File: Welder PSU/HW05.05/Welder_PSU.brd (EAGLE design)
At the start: 0 parts

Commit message: Welder PSU HW05.05 Altium -> Eagle Ongoing
Recreating schematic done, Netlisting Ongoing
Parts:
- added C1, C10, C11, C15, C18, C19, C2, C200, C203, C206, C210, C3, C305, C317, C318, C320, C323, C324, C328, C329, C332, C333, C334, C335, C343, C346, C347, C348, C349, C354, C366, C368, C4, C400, C401, C402, C412, C439, C440, C441, C442, C443, C444, C445, C446, C447, C449, C450, C451, C452, C456, C457, C5, C500, C501, C502, C503, C504, C505, C506, C6, C7: 100nF/50V, Labops_Lib_AH:EIA0603
- added C100, C101, C103, C104, C105, C106: SLP152M250H9P3, Labops_Lib_AH:CAPACITOR-ELKO-400V-RM10-35X50
- added C102: R49AN347050B1M, Labops_Lib_AH:R49AN347050B1M
- added C108: ERP610W471MEF0, Labops_Lib_AH:CAP-P12.5-H15-W4-D1
- added C12, C22, C336, C339, C355, C358, C367, C386, C390, C391, C392, C398, C399, C427, C428, C430, C431, C432, C435, C436: 10uF/35V, Labops_Lib_AH:EIA0603
- added C201, C202, C205, C207, C211: 50PX470MEFC10X20, Labops_Lib_AH:CAPACITOR-ELKO-RM5-10X16
- added C300, C351, C352, C353: 470pF/50V, Labops_Lib_AH:EIA0603
- added C301, C311: 12pF/50V, Labops_Lib_AH:EIA0603
- added C302, C312: 510pF/50V, Labops_Lib_AH:EIA0603
- added C303, C304, C307, C308: HVCC153Y6P471MEAX, Labops_Lib_AH:CAPACITOR-FILM-RM12.5MM-12MM
- added C306, C423, C424, C425, C426: 330pF/50V, Labops_Lib_AH:EIA0603
- added C313, C316, C421: 10nF/50V, Labops_Lib_AH:EIA0603
- added C314, C342, C345, C362, C365: 1nF/50V, Labops_Lib_AH:EIA0603
- added C315: 22uF/16V, Labops_Lib_AH:EIA0603
- added C319, C325, C422: 1uF/25V, Labops_Lib_AH:EIA0603
- added C330, C357, C413, C414, C415, C418: 100nF/100V, Labops_Lib_AH:EIA0603
- added C331, C388, C389, C395, C396, C397, C416, C417, C429: 10uF/25V, Labops_Lib_AH:EIA0603
- added C340, C356, C409, C410: 4.7uF/50V, Labops_Lib_AH:EIA0603
- added C344, C453: 1uF/50V, Labops_Lib_AH:EIA0603
- added C350, C369: 2.2uF/35V, Labops_Lib_AH:EIA0603
- added C359, C385: 100nF/25V, Labops_Lib_AH:EIA0603
- added C370, C371, C372, C373, C374, C375, C376, C377, C378, C379, C380, C381: 100pF/50V, Labops_Lib_AH:EIA0603
- added C382, C394: 10F/35V, Labops_Lib_AH:EIA0603
- added C383, C433: 100pF/25V, Labops_Lib_AH:EIA0603
- added C384: 4.7uF/35V, Labops_Lib_AH:EIA0603
- added C393: 470uF/35V, Labops_Lib_AH:CAPACITOR-ELKO-RM5-10X16
- added C419, C420: CK45-B3FD102KYVNA, Labops_Lib_AH:C_DISC_P7.5D12
- added C437, C438: ECW-F4245JLB, Labops_Lib_AH:CAPACITOR-FILM-RM17.5-28X17.5X25
- added C448, C454, C455: 1uF/35V, Labops_Lib_AH:EIA0603
- added C458: 10uF/16V, Labops_Lib_AH:EIA0603
- added D1, D315, D317, D319, D320, D322: SD103AW, Labops_Lib_AH:SOD-323
- added D100, D103: RS1M-13-F, Labops_Lib_AH:SMA-DIODE
- added D101: GBPC3510W, Labops_Lib_AH:GBPC3510W
- added D102: 1N5387BRLG, Labops_Lib_AH:DO-201AD
- added D104, D105: 1N4739A, Labops_Lib_AH:DO-201AD
- added D2, D302, D316, D318: SS14, Labops_Lib_AH:SMA
- added D200, D201: 26-21/GPC-F3138B/CA, Labops_Lib_AH:SMD1206-LED
- added D300, D303, D304, D305, D323, D4: STTH1R04USMB, Labops_Lib_AH:SMB
- added D307, D308, D309, D310, D311, D312: FEP30DP-E3/45TO-247AD, Labops_Lib_AH:TO-247AD
- added D313, D413: GB02SLT12-214, Labops_Lib_AH:SMB
- added D324: BAT54S, Labops_Lib_AH:SOT23DUALDIODE
- added IC1: UCC28951PWR, Labops_Lib_AH:TSSOP24
- added IC100: PC817, Labops_Lib_AH:DIP04
- added IC2, IC301, IC302: LMV641, Labops_Lib_AH:SOT-23-5
- added IC306, IC307, IC310, IC311: UCC21710, Labops_Lib_AH:SOIC16_WIDE_HV
- added IC308, IC309: MAX764CSA+, Labops_Lib_AH:SOIC8
- added IC312, IC313: LM317AEMP, Labops_Lib_AH:SOT223_LM317AEMP
- added IC401: CSTNE8M00G520000R0, Labops_Lib_AH:CSTNE8M00G520000R0
- added IC500: SN65HVD3082EDR, Labops_Lib_AH:SOIC8
- added K100, K101: PANASONIC_ALFG2PF09PANASONIC_ALFG2PF09_0_0, Labops_Lib_AH:PANASONIC_ALFG2PF09_0
- added L300, L302, L304, L308, L309: BLM18RK601SN1D, Labops_Lib_AH:0603
- added L303, L307: SRN8040TA-220M, Labops_Lib_AH:SRN8040TA-220M
- added Q1, Q2, Q300, Q306, Q307, Q308, Q309, Q310, T500, T501, T502: 2N7002, Labops_Lib_AH:SOT23
- added Q100: BC640TA, Labops_Lib_AH:TO-92
- added Q101: KSD1616AYTA, Labops_Lib_AH:TO-92
- added Q500, Q502, Q504: DMP6185SEQ-13, Labops_Lib_AH:SOT223
- added Q501, Q503, Q505, Q506, Q507: BC817, Labops_Lib_AH:SOT23
- added R1, R11, R12, R4, R447, R448, R5, R502, R506, R508, R511, R513, R517, R518, R521, R523, R524, R528: 100R 1%, Labops_Lib_AH:EIA0603
- added R10, R14, R2, R305, R306, R307, R336, R350, R351, R363, R366, R386, R388, R449, R463, R500, R501, R503, R505, R507, R510, R512, R514, R515, R516, R519, R6: 10K 1%, Labops_Lib_AH:EIA0603
- added R100, R112: B57364S100M54, Labops_Lib_AH:VARISTOR_D25_P7.5
- added R101, R103, R111: R_1206EIA1206, Labops_Lib_AH:EIA1206
- added R102, R104: ERG-2SJ513, Labops_Lib_AH:ERG-2S
- added R105: 82K 1%, Labops_Lib_AH:R2010
- added R106: 0R, Labops_Lib_AH:EIA0603
- added R107, R109: 330R 1%, Labops_Lib_AH:EIA0603
- added R108, R113: R_2010EIA2010, Labops_Lib_AH:EIA2010
- added R110: 220K 1%, Labops_Lib_AH:EIA0603
- added R114, R115, R326, R398: RNF12FTD10M0, Labops_Lib_AH:RES-RM12.5-VR37
- added R13, R353, R361, R373, R379, R381, R526, R527: 0R 1%, Labops_Lib_AH:EIA0603
- added R200, R309, R312, R315, R328, R331, R349, R504, R509: 1K 1%, Labops_Lib_AH:EIA0603
- added R201, R3, R346, R347, R348, R391, R8, R9: 3.3K 1%, Labops_Lib_AH:EIA0603
- added R29, R30, R308, R390, R408, R409, R420, R421: 4.7k 1%, Labops_Lib_AH:EIA0603
- added R300, R334, R345, R365, R368: 100K 1%, Labops_Lib_AH:EIA0603
- added R301, R302, R310, R311, R322, R323, R329, R330: 47R 1%, rcl:R2512
- added R303, R31, R407, R419: 4.7K 1%, Labops_Lib_AH:EIA0603
- added R304, R313, R325, R332, R387, R396: 33R 1%, Labops_Lib_AH:EIA2010
- added R314, R343, R400, R403: 10k 1%, Labops_Lib_AH:EIA0603
- added R316: 12R 1%, Labops_Lib_AH:EIA2512
- added R327, R385: 22R 1%, Labops_Lib_AH:EIA2010
- added R333, R369: 150K 1%, Labops_Lib_AH:EIA0603
- added R335, R344: 1.5K 1%, Labops_Lib_AH:EIA0603
- added R337, R341: 510R 1%, Labops_Lib_AH:EIA0603
- added R338, R399, R402: 33K 1%, Labops_Lib_AH:EIA0603
- added R339: 162R 1%, Labops_Lib_AH:EIA0603
- added R340: WSL5931L3000FEA, Labops_Lib_AH:WSLP3921
- added R342: 220k 1%, Labops_Lib_AH:EIA0603
- added R352, R354, R358, R370, R380, R384, R461, R462, R7: 10R 1%, Labops_Lib_AH:EIA0603
- added R355, R364, R377, R382, R430, R431: 412R 1%, Labops_Lib_AH:EIA0603
- added R356, R367, R378, R383, R438: 1.2K 1%, Labops_Lib_AH:EIA0603
- added R357, R359: 49.9K 1%, Labops_Lib_AH:EIA0603
- added R360, R362: 65K 1%, Labops_Lib_AH:EIA0603
- added R371, R374: 18K 1%, Labops_Lib_AH:EIA0603
- added R372, R401, R424, R427: 10R 1%, Labops_Lib_AH:EIA2512
- added R375, R376: 620R 1%, Labops_Lib_AH:EIA0603
- added R389: 825K 1%, Labops_Lib_AH:EIA0603
- added R397, R406, R412, R418, R425, R428: 5.6K 1%, Labops_Lib_AH:EIA0603
- added R404, R410, R416, R422: 220R 1%, Labops_Lib_AH:EIA0603
- added R405, R411, R417, R423: 2.2K 1%, Labops_Lib_AH:EIA0603
- added R426, R429: 5.6k 1%, Labops_Lib_AH:EIA0603
- added R432, R433: 3.9K 1%, Labops_Lib_AH:EIA0603
- added R434, R435: 15.8K 1%, Labops_Lib_AH:EIA0603
- added R436: 41K 1%, Labops_Lib_AH:EIA0603
- added R439, R440, R441, R442: RR02J22RTB, Labops_Lib_AH:RES-RM15-RSF1W
- added R520, R522, R525: 470R 1%, Labops_Lib_AH:EIA0603
- added T1: CST206-2A, Labops_Lib_AH:CST206-2A
- added T300, T301, T303, T304: IHW20N120R5, Labops_Lib_AH:TO-247AC
- added TR305: 11-0060-A, Labops_Lib_AH:11-0060-A
- added U2: R7FA6M5BG3CFBLQFP-144-M, Labops_Lib_AH:LQFP-144-M
- added U300, U301: PAD_3MMX6MM, Labops_Lib_AH:PAD-3.0X6.0MM
- added V1, V2, V3, V500, V501, V502, V503, V504: 0603ESDA-24NSMD, Labops_Lib_AH:EIA0603
- added V100, V300: B72205S0271K101B72205S2131K101, Labops_Lib_AH:EPCOS_B72205S0271K101_0
- added X1: WF2549-2WS05S0B01, Labops_Lib_AH:X10_100MIL_2XROW_VERT
- added X100, X101: 01020071Z, Labops_Lib_AH:FUSE_CLIP_01020071Z
- added X200, X201, X202, X203: 726386-2TE_726386-2, Labops_Lib_AH:TE_726386-2
- added X204, X205: MOLEX_206832-0601MOLEX_206832-0601, Labops_Lib_AH:MOLEX_206832-0601
- added X400, X401, X402: 2304-6111-TP, Labops_Lib_AH:X04_100MIL
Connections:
- new net /COMM_RX_EN: R520.2
- new net /DO_COMM_RX_EN: U2.35
- new net /G_DRV_FAULTA: C371.2, IC306.13, R308.2
- new net /G_DRV_FAULTB: C374.2, IC307.13, R408.2
- new net /G_DRV_FAULTC: C377.2, IC310.13, R30.2
- new net /G_DRV_FAULTD: C380.2, IC311.13, R420.2
- new net AI_I_OUT: U2.113
- new net AN_OUTA_H: IC306.4, R325.2
- new net AN_OUTA_L: IC306.6, R327.2
- new net AN_OUTB_H: IC307.4, R304.2
- new net AN_OUTB_L: IC307.6, R313.2
- new net AN_OUTC_H: IC310.4, R332.2
- new net AN_OUTC_L: IC310.6, R385.2
- new net AN_OUTD_H: IC311.4, R387.2
- new net AN_OUTD_L: IC311.6, R396.2
- new net A_I_OUT: C433.2, IC301.1, R339.1, R345.2
- new net BCD_A: C500.1, Q501.3
- new net BCD_B: C501.1, Q503.3
- new net BCD_C: C502.1, Q505.3
- new net BCD_D: C506.1, Q507.3
- new net COMM_TX_EN: R522.2
- new net CTRLR_OUTA: IC1.22, R358.1
- new net CTRLR_OUTB: IC1.21, R370.1
- new net CTRLR_OUTC: IC1.20, R380.1
- new net CTRLR_OUTD: IC1.19, R384.1
- new net DBG_TDI: X1.1
- new net DGB_SWDCLK_TCK: U2.72
- new net DGB_SWDIO_TCK: X1.7
- new net DGB_SWDIO_TDO: U2.74
- new net DGB_SWDIO_TMS: U2.73, X1.5
- new net DGB_SWO_TDO: X1.3
- new net DISP1_VCC: Q504.2, Q504.4, V502.2
- new net DISP2_VCC: Q502.2, Q502.4, V501.2
- new net DISP3_VCC: Q500.2, Q500.4, V500.2
- new net DI_G_DRV_RDY: C370.2, C376.2, C400.2, IC306.12, IC310.12, R303.2, R31.2, R448.1, U2.85, X400.2
- new net DI_G_DRV_REDY: C373.2, C379.2, IC307.12, IC311.12, R407.2, R419.2
- new net DI_UART_RX: U2.32
- new net DO_7SEG_BCD_A: R504.2, U2.71
- new net DO_7SEG_BCD_B: R509.2, U2.70
- new net DO_7SEG_BCD_C: R513.2, U2.69
- new net DO_7SEG_BCD_D: U2.66
- new net DO_7SEG_DISP1_EN: R517.2, U2.65
- new net DO_7SEG_DISP2_EN: R508.2, U2.64
- new net DO_7SEG_DISP3_EN: R502.2, U2.63
- new net DO_ABRUPT_I_OFF: R462.1, U2.118
- new net DO_COMM_TX_EN: U2.34
- new net DO_I_SET_PWM: U2.97, V3.2, X401.2
- new net DO_PSFB_CTRL_ON: U2.98
- new net DO_PWM_I_SET: R349.1, R7.1
- new net DO_UART_TX: U2.33
- new net DO_V_SET_PWM: V2.2, X401.3
- new net D_7SEG_BCD_D: R524.2
- new net EA_IN: D2.2, D302.2, R305.2, R336.2, R461.1
- new net GND: C1.1, C10.1, C108.P$1, C11.1, C15.1, C18.1, C19.1, C2.1, C200.1, C201.2, C202.2, C203.1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
- new net GND1: C3.2, C346.2, C4.2, IC2.2, Q2.2, R10.1, R6.1
- new net GND_AUX: C206.1, C207.2, C210.1, C211.1, D200.2, X205.5
- new net G_DRV1_VCC: C332.2, C333.2, IC306.15, L302.2, R303.1, R308.1, R390.1
- new net G_DRV2_VCC: C343.2, C344.2, IC307.15, L304.2, R407.1, R408.1, R409.1
- new net G_DRV3_VCC: C10.2, C11.2, IC310.15, L308.2, R29.1, R30.1, R31.1
- new net G_DRV4_VCC: C18.2, C19.2, IC311.15, L309.2, R419.1, R420.1, R421.1
- new net G_DRV_INA: IC306.10, R353.1, R355.1
- new net G_DRV_INB: IC307.10, R361.1, R364.1
- new net G_DRV_INC: IC310.10, R373.1, R377.1
- new net G_DRV_IND: IC311.10, R381.1, R382.1
- new net MAINS_L: V100.2, X100.1, X100.1-1
- new net MAINS_L_FUSED: C102.2, D101.2, R101.2, X101.1, X101.1-1, X200.1, X200.1-2, X201.1, X201.1-2
- new net MAINS_N: C102.1, C108.P$2, D101.4, R103.1, R114.2, V100.1, X202.1, X202.1-2, X203.1, X203.1-2
- new net N$1: C311.1, C315.2, IC302.4, R333.1, R338.2
- new net N$10: IC1.3, R354.2
- new net N$100: Q100.3, R109.1
- new net N$101: D105.K, Q101.3, R111.2
- new net N$102: IC100.4, R106.2, R109.2
- new net N$103: C103.2, C104.2, C106.2, D101.3, R104.1
- new net N$104: C100.2, C101.2, C103.1, C104.1, C105.2, C106.1
- new net N$105: D201.1, R201.1
- new net N$106: D104.K, R105.1, R107.2
- new net N$107: D200.1, R200.1
- new net N$108: D102.A, R105.2
- new net N$109: D100.C, D102.K
- new net N$11: C324.2, IC1.5
- new net N$110: IC100.1, R107.1, R110.2
- new net N$111: C451.2, U2.15
- new net N$112: C454.1, C456.1, U2.127
- new net N$113: C452.1, U2.92
- new net N$114: IC401.3, R14.2, U2.20
- new net N$115: IC401.1, R13.2, R14.1
- new net N$116: R13.1, U2.19
- new net N$117: C505.2, R521.2, R523.2
- new net N$119: IC500.1, Q506.2
- new net N$12: IC1.2, R352.2
- new net N$120: Q506.1, R516.2
- new net N$121: Q501.1, R504.1
- new net N$123: IC500.2, R520.1
- new net N$124: Q501.2, R506.2
- new net N$125: X1.8
- new net N$127: IC500.3, R522.1
- new net N$128: IC500.4, R525.1
- new net N$129: Q503.1, R509.1
- new net N$13: C320.2, C422.1, IC1.23, L300.1
- new net N$131: Q503.2, R511.2
- new net N$133: Q505.1, R513.1
- new net N$135: Q505.2, R518.2
- new net N$137: Q507.1, R524.1
- new net N$139: Q507.2, R528.2
- new net N$14: IC1.16, R386.1
- new net N$140: R508.1, R510.2, T501.1
- new net N$141: R502.1, R503.2, T500.1
- new net N$142: R501.1, T500.3
- new net N$143: Q500.1, R500.1, R501.2
- new net N$145: R507.1, T501.3
- new net N$147: Q502.1, R505.1, R507.2
- new net N$15: D303.K, R315.1, R316.2
- new net N$150: R517.1, R519.2, T502.1
- new net N$151: R514.1, T502.3
- new net N$152: Q504.1, R512.1, R514.2
- new net N$16: Q307.1, R356.1, R358.2
- new net N$17: IC1.13, R366.2, R375.1
- new net N$18: Q307.2, R353.2, R356.2
- new net N$19: IC1.14, R363.2, R376.1
- new net N$2: IC1.12, R374.2, R379.2
- new net N$20: C421.2, R338.1, R339.2, R342.1, R343.1
- new net N$21: D303.A, T1.2
- new net N$22: Q309.1, R378.1, R380.2
- new net N$23: Q309.2, R373.2, R378.2
- new net N$24: C313.2, R335.2, R337.1
- new net N$25: C313.1, C314.1, C316.2
- new net N$26: C316.1, R341.1, R344.2
- new net N$27: Q308.1, R367.1, R370.2
- new net N$28: Q308.2, R361.2, R367.2
- new net N$29: R323.1, R330.2
- new net N$3: IC1.11, R369.1, R371.1
- new net N$30: C433.1, IC301.4, R341.2, R345.1
- new net N$31: Q306.1, R349.2, R351.2
- new net N$32: C383.2, IC301.3, R334.1, R337.2
- new net N$33: Q310.1, R383.1, R384.2
- new net N$34: R301.1, R310.2
- new net N$35: Q310.2, R381.2, R383.2
- new net N$36: C303.2, R301.2
- new net N$37: C315.1, R342.2
- new net N$38: Q1.1, R462.2, R463.2
- new net N$39: Q306.3, R347.2, R348.1
- new net N$4: IC1.10, R365.1, R368.1
- new net N$40: R302.1, R311.2
- new net N$41: C304.2, R302.2
- new net N$42: C352.1, R330.1, R331.2, T303.3
- new net N$43: R322.1, R329.2
- new net N$44: C307.2, R322.2
- new net N$45: C308.2, R323.2
- new net N$46: C318.1, R346.2, R347.1
- new net N$47: C437.2, C438.2, TR305.1
- new net N$48: D310.1, D310.3, D311.1, D311.3, D312.1, D312.3, TR305.3
- new net N$49: D307.1, D307.3, D308.1, D308.3, D309.1, D309.3, TR305.5
- new net N$5: IC1.9, R362.1
- new net N$50: R440.2
- new net N$51: R439.2, R440.1
- new net N$52: C419.1, R439.1
- new net N$53: C420.1, R442.2
- new net N$54: R441.1
- new net N$55: R441.2, R442.1
- new net N$56: D413.A, R401.1, R427.1
- new net N$57: C317.1, IC302.3, R346.1, R350.2
- new net N$58: IC309.2, R402.2, R403.2
- new net N$59: C423.2, R397.2, R404.2, R425.1
- new net N$6: IC1.8, R360.1
- new net N$60: IC312.1, R430.1, R432.1
- new net N$61: C359.1, IC309.4, R403.1
- new net N$62: IC313.1, R431.1, R433.1
- new net N$63: D318.1, IC309.8, L307.2
- new net N$64: D316.1, IC308.8, L303.2
- new net N$65: C354.1, IC308.4, R400.1
- new net N$66: IC308.2, R399.2, R400.2
- new net N$67: C396.2, C397.2
- new net N$68: D300.A, R404.1
- new net N$69: C424.2, R406.2, R410.2, R426.1
- new net N$7: IC1.6, R357.1
- new net N$70: D313.A, R372.1, R424.1
- new net N$71: C425.2, R412.1, R416.2, R428.2
- new net N$72: D304.A, R416.1
- new net N$73: D4.A, R410.1
- new net N$74: C312.1, R333.2
- new net N$75: R306.1, R307.2, R314.1
- new net N$76: Q1.3, R461.2
- new net N$77: C311.2, C312.2, D2.1, IC302.1, R336.1
- new net N$78: C305.1, R314.2
- new net N$79: Q2.1, R6.2, R7.2
- new net N$8: IC1.7, R359.1
- new net N$80: Q2.3, R3.1, R8.2
- new net N$81: C3.1, R8.1, R9.2
- new net N$82: C4.1, IC2.3, R10.2, R9.1
- new net N$83: C426.2, R418.2, R422.2, R429.1
- new net N$84: D305.A, R422.1
- new net N$85: C301.1, C305.2, IC2.4, R300.1, R306.2
- new net N$86: C302.1, R300.2
- new net N$87: C301.2, C302.2, D302.1, IC2.1, R305.1
- new net N$88: C416.1, R307.1, R434.2
- new net N$89: C417.1, R2.1, R434.1, R435.1
- new net N$9: IC1.4, R354.1
- new net N$90: R435.2, R436.2, R438.2
- new net N$91: R114.1, R115.2
- new net N$92: D323.K, R436.1
- new net N$93: D101.1, K100.4, K101.4, R100.1, R112.1
- new net N$94: C415.2, C418.1
- new net N$95: D103.C, K100.2, K101.2, Q101.1
- new net N$96: R101.1, R103.2
- new net N$97: D103.A, K100.1, K101.1, Q100.1, R106.1
- new net N$98: Q101.2, R108.2, R113.2
- new net N$99: R102.1, R104.2
- new net NDI_G_DRV_FAULTA: C1.2, R4.1, U2.89, X402.1
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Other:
- board outline added: 160 x 100 mm

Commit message: Welder PSU HW05.05
Translated to Eagle, Design Rule Check still open
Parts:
- removed C1, C10, C11, C15, C18, C19, C2, C3, C4, C5, C6, C7: 100nF/50V, Labops_Lib_AH:EIA0603
- removed C12, C22: 10uF/35V, Labops_Lib_AH:EIA0603
- removed D1: SD103AW, Labops_Lib_AH:SOD-323
- removed D2: SS14, Labops_Lib_AH:SMA
- removed D4: STTH1R04USMB, Labops_Lib_AH:SMB
- removed D413: GB02SLT12-214, Labops_Lib_AH:SMB
- removed IC2: LMV641, Labops_Lib_AH:SOT-23-5
- removed Q1, Q2, Q307, Q308, Q309, Q310: 2N7002, Labops_Lib_AH:SOT23
- removed R1, R11, R12, R4, R5: 100R 1%, Labops_Lib_AH:EIA0603
- removed R10, R14, R2, R6: 10K 1%, Labops_Lib_AH:EIA0603
- removed R13: 0R 1%, Labops_Lib_AH:EIA0603
- removed R29, R30: 4.7k 1%, Labops_Lib_AH:EIA0603
- removed R3, R8, R9: 3.3K 1%, Labops_Lib_AH:EIA0603
- removed R31: 4.7K 1%, Labops_Lib_AH:EIA0603
- removed R7: 10R 1%, Labops_Lib_AH:EIA0603
- removed T1: CST206-2A, Labops_Lib_AH:CST206-2A
- removed U2: R7FA6M5BG3CFBLQFP-144-M, Labops_Lib_AH:LQFP-144-M
- removed V1, V2, V3: 0603ESDA-24NSMD, Labops_Lib_AH:EIA0603
- added C204, C309, C310, C338, C361, C363, C364, C403, C404, C405, C407, C411: 100nF/50V, Labops_Lib_AH:EIA0603
- added C337: 1uF/25V, Labops_Lib_AH:EIA0603
- added C360: 1uF/35V, Labops_Lib_AH:EIA0603
- added C387: 100nF/100V, Labops_Lib_AH:EIA0603
- added C408, C434: 10uF/35V, Labops_Lib_AH:EIA0603
- added D301: STTH1R04USMB, Labops_Lib_AH:SMB
- added D306: SS14, Labops_Lib_AH:SMA
- added D314: GB02SLT12-214, Labops_Lib_AH:SMB
- added D321: SD103AW, Labops_Lib_AH:SOD-323
- added IC300: LMV641, Labops_Lib_AH:SOT-23-5
- added IC400: R7FA6M5BG3CFBLQFP-144-M, Labops_Lib_AH:LQFP-144-M
- added R317, R318, R319, R320, R321, R324, R450: 10K 1%, Labops_Lib_AH:EIA0603
- added R413: 4.7K 1%, Labops_Lib_AH:EIA0603
- added R414, R415: 4.7k 1%, Labops_Lib_AH:EIA0603
- added R437: 100K 1%, Labops_Lib_AH:EIA0603
- added R443, R444, R445, R446, R452: 100R 1%, Labops_Lib_AH:EIA0603
- added R451: 0R 1%, Labops_Lib_AH:EIA0603
- added T302, T307, T308, T309, T310, T313: 2N7002, Labops_Lib_AH:SOT23
- added TR300: CST206-2A, Labops_Lib_AH:CST206-2A
- added V400, V401, V402: 0603ESDA-24NSMD, Labops_Lib_AH:EIA0603
- added X2, X4: 7461061, Labops_Lib_AH:X01_M10_7461061
- added X3: 726386-2TE_726386-2, Labops_Lib_AH:TE_726386-2
- added X403: WF2549-2WS05S0B01, Labops_Lib_AH:X10_100MIL_2XROW_VERT
- added X5, X6: 615008148521, Labops_Lib_AH:615008148521
- added X7, X8: 2304-6111-TP, Labops_Lib_AH:X04_100MIL
- C108: device Labops_Lib_AH:CAP-P12.5-H15-W4-D1 -> Labops_Lib_AH:CAPACITOR-FILM-RM12.5MM-12MM
- R309, R312, R328, R331, R436, R438: device Labops_Lib_AH:EIA0603 -> Labops_Lib_AH:EIA2010
- X1: value WF2549-2WS05S0B01 -> 726386-2TE_726386-2; device Labops_Lib_AH:X10_100MIL_2XROW_VERT -> Labops_Lib_AH:TE_726386-2
- moved R340 624.7 mm to (348.9, 16.9), turned to 180 degrees
- moved V300 591.8 mm to (297.1, 11.8), turned to 180 degrees
- moved R439 581.2 mm to (256.0, 48.3), turned to 90 degrees
- moved V502 581.0 mm to (189.7, 5.24)
- moved V501 578.4 mm to (181.1, 5.24)
- moved R512 577.3 mm to (185.3, 11.1), turned to 90 degrees
- moved V500 576.0 mm to (172.4, 5.24)
- moved R514 567.3 mm to (185.3, 7.78), turned to 90 degrees
- moved Q504 562.8 mm to (189.6, 10.3)
- moved R519 554.2 mm to (163.5, 7.53), turned to 270 degrees
- moved R505 549.3 mm to (176.7, 11.1), turned to 90 degrees
- moved R517 547.3 mm to (165.1, 7.53), turned to 90 degrees
- moved R507 539.8 mm to (176.7, 7.78), turned to 90 degrees
- moved Q502 535.7 mm to (181.0, 10.3)
- moved C352 535.2 mm to (262.8, 140.0), turned to 90 degrees
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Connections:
- net VDC360V renamed NODE-A
- removed net /COMM_RX_EN: R520.2
- removed net A_I_OUT: C433.2, IC301.1, R339.1, R345.2
- removed net COMM_TX_EN: R522.2
- removed net DGB_SWDCLK_TCK: U2.72
- removed net DGB_SWO_TDO: X1.3
- removed net DI_G_DRV_REDY: C373.2, C379.2, IC307.12, IC311.12, R407.2, R419.2
- removed net DO_PWM_I_SET: R349.1, R7.1
- removed net D_7SEG_BCD_D: R524.2
- removed net GND1: C3.2, C346.2, C4.2, IC2.2, Q2.2, R10.1, R6.1
- removed net GND_AUX: C206.1, C207.2, C210.1, C211.1, D200.2, X205.5
- removed net N$125: X1.8
- removed net N$50: R440.2
- removed net N$54: R441.1
- removed net N$99: R102.1, R104.2
- removed net NDI_G_DRV_FAULTA: C1.2, R4.1, U2.89, X402.1
- removed net NDI_G_DRV_FAULTB: C2.2, R5.1, U2.88, X402.2
- removed net NDI_G_DRV_FAULTC: C5.2, R11.1, U2.87, X402.3
- removed net NDI_G_DRV_FAULTD: C6.2, R12.1, U2.86, X402.4
- removed net NODE_B: C335.1, C336.1, C345.1, C349.1, C350.1, C382.1, C392.1, C424.1, D317.A, IC307.3, R411.2
- removed net NODE_D: C22.1, C365.1, C366.1, C367.1, C368.1, C369.1, C393.2, C394.1, C426.1, D320.A, IC311.3, R423.2
- removed net UART_RX: Q506.3, R515.2
- removed net UART_TX: R525.2
- removed net VDD_B: R406.1
- removed net VDD_D: R418.1
- removed net VEE_B: C349.2, C350.2, C392.2, IC307.8
- removed net VEE_D: C22.2, C368.2, C369.2, IC311.8
- removed net V_RECT_F_MIN: D104.A, IC100.2, R110.1
- new net N$118: IC307.1
- net /DO_COMM_RX_EN: now also IC400.32, R520.2; no longer U2.35
- net /G_DRV_FAULTA: now also C404.2, IC400.89, R445.1, X402.1
- net /G_DRV_FAULTB: now also C405.2, IC400.88, R443.1, X402.2
- net /G_DRV_FAULTC: now also C403.2, IC400.87, R414.2, R446.1, X402.3; no longer R30.2
- net /G_DRV_FAULTD: now also C407.2, IC400.86, R444.1, X402.4
- net AI_I_OUT: now also C433.2, IC301.1, IC400.113, R339.1, R345.2; no longer U2.113
- net BCD_A: now also X8.1
- net BCD_B: now also X8.2
- net BCD_C: now also X8.3
- net BCD_D: now also X8.4
- net DBG_TDI: now also IC400.75, X403.1; no longer X1.1
- net DGB_SWDIO_TCK: now also IC400.72, X403.7; no longer X1.7
- net DGB_SWDIO_TDO: now also IC400.74, X403.3; no longer U2.74
- net DGB_SWDIO_TMS: now also IC400.73, X403.5; no longer U2.73, X1.5
- net DISP1_VCC: now also X7.1
- net DISP2_VCC: now also X7.2
- net DISP3_VCC: now also X7.3
- net DI_G_DRV_RDY: now also C373.2, C379.2, IC307.12, IC311.12, IC400.85, R407.2, R413.2, R419.2; no longer R31.2, U2.85
- net DI_UART_RX: now also IC400.35, Q506.3, R515.2; no longer U2.32
- net DO_7SEG_BCD_A: now also IC400.71; no longer U2.71
- net DO_7SEG_BCD_B: now also IC400.70; no longer U2.70
- net DO_7SEG_BCD_C: now also IC400.69; no longer U2.69
- net DO_7SEG_BCD_D: now also IC400.66, R524.2; no longer U2.66
- net DO_7SEG_DISP1_EN: now also IC400.65; no longer U2.65
- net DO_7SEG_DISP2_EN: now also IC400.64; no longer U2.64
- net DO_7SEG_DISP3_EN: now also IC400.63; no longer U2.63
- net DO_ABRUPT_I_OFF: now also IC400.118; no longer U2.118
- net DO_COMM_TX_EN: now also IC400.33, R522.2; no longer U2.34
- net DO_I_SET_PWM: now also IC400.97, R349.1, V401.2; no longer U2.97, V3.2
- net DO_PSFB_CTRL_ON: now also IC400.98; no longer U2.98
- net DO_UART_TX: now also IC400.34, R525.2; no longer U2.33
- net DO_V_SET_PWM: now also R320.1, V402.2; no longer V2.2
- net EA_IN: now also D306.2; no longer D2.2
- net GND: now also C108.1, C204.1, C309.2, C310.2, C337.2, C338.1, C346.2, C360.1, C361.1, C363.1, C364.1, C403.1, C404.1, C405.1, C407.1, IC300.2, IC400.100, IC400.112, IC400.122, IC400.125, IC400.128, IC400.141, IC400.18, IC400.48, IC400.67, IC400.82, IC400.91, R201.1, R321.1, R324.1, R437.2, T302.2, T313.2, TR300.1, V400.1, V401.1, V402.1, X403.10, X403.6, X403.8, X7.4; no longer C1.1, C10.1, C108.P$1, C11.1, C15.1, C18.1, C19.1, C2.1, C5.1, C6.1, D201.2, Q1.2, R2.2, T1.1, U2.100, U2.112, U2.122, U2.125, U2.128, U2.141, U2.18, U2.48, U2.67, U2.82, U2.91, V1.1, V2.1, V3.1, X1.10, X1.6
- net G_DRV3_VCC: now also C360.2, C361.2, R413.1, R414.1, R415.1; no longer C10.2, C11.2, R29.1, R30.1, R31.1
- net G_DRV4_VCC: now also C363.2, C364.2; no longer C18.2, C19.2
- net MAINS_L: now also X1.1, X1.1-2
- net MAINS_N: now also C108.2, X3.1, X3.1-2; no longer C108.P$2
- net N$103: now also IC311.1; no longer C103.2, C104.2, C106.2, D101.3, R104.1
- net N$104: now also R102.1, R104.2
- net N$105: now also IC306.1; no longer D201.1, R201.1
- net N$107: now also D200.2, R200.2; no longer D200.1, R200.1
- net N$11: now also D201.2, R201.2; no longer C324.2, IC1.5
- net N$111: now also IC400.15; no longer U2.15
- net N$112: now also X205.3; no longer C454.1, C456.1, U2.127
- net N$113: now also IC400.92; no longer U2.92
- net N$114: now also IC400.20, R450.2; no longer R14.2, U2.20
- net N$115: now also R451.2; no longer R13.2, R14.1
- net N$116: now also IC400.19, R450.1, R451.1; no longer R13.1, U2.19
- net N$16: now also T307.1; no longer Q307.1
- net N$18: now also T307.2; no longer Q307.2
- net N$21: now also TR300.2; no longer T1.2
- net N$22: now also T309.1; no longer Q309.1
- net N$23: now also T309.2; no longer Q309.2
- net N$27: now also T308.1; no longer Q308.1
- net N$28: now also T308.2; no longer Q308.2
- net N$33: now also T310.1; no longer Q310.1
- net N$35: now also T310.2; no longer Q310.2
- net N$38: now also T313.1; no longer Q1.1
- net N$42: now also X205.2; no longer C352.1, R330.1, R331.2, T303.3
- net N$48: now also R441.1
- net N$49: now also R440.2
- net N$56: now also D314.A; no longer D413.A
- net N$67: now also X205.4; no longer C396.2, C397.2
- net N$70: now also C387.1
- net N$73: now also D301.A; no longer D4.A
- net N$76: now also T313.3; no longer Q1.3
- net N$77: now also D306.1; no longer D2.1
- net N$79: now also R320.2, R324.2, T302.1; no longer Q2.1, R6.2, R7.2
- net N$80: now also R318.2, R319.1, T302.3; no longer Q2.3, R3.1, R8.2
- net N$81: now also C310.1, R317.2, R318.1; no longer C3.1, R8.1, R9.2
- net N$82: now also C309.1, IC300.3, R317.1, R321.2; no longer C4.1, IC2.3, R10.2, R9.1
- net N$85: now also IC300.4; no longer IC2.4
- net N$87: now also IC300.1; no longer IC2.1
- net N$89: now also R437.1; no longer R2.1
- net NDO_G_DRV_RST: now also C401.2, IC400.93, R415.2; no longer C402.2, R29.2, U2.93
- net NDO_PSFB_CTRL_ON: now also R452.2; no longer R1.2
- net NODE_A: now also C411.1, D301.K, IC308.3, R309.1; no longer C7.1, D4.K, R309.2
- net NODE_C: now also C434.1, R312.1; no longer C12.1, R312.2
- net NRST: now also IC400.55, X403.9; no longer U2.55, X1.9
- net PSFB_EN: now also R452.1, V400.2; no longer R1.1, V1.2
- net QA_GATE: now also R309.2; no longer R309.1
- net QB_GATE: now also R328.2; no longer R328.1
- net QC_GATE: now also R312.2; no longer R312.1
- net QD_GATE: now also R331.2; no longer R331.1
- net RS485-A: now also X5.1
- net RS485-A-NEXT: now also X6.1
- net RS485-B: now also X5.2
- net RS485-B-NEXT: now also X6.2
- net SS-EN: now also C324.2, IC1.5
- net VBATT: now also IC400.14; no longer U2.14
- net VCC_USBHS: now also IC400.40; no longer U2.40
- net VDDA_REG: now also C388.2, C389.2, D321.A, IC306.5; no longer D1.A
- net VDDC_REG: now also C434.2; no longer C12.2, C388.2, C389.2, IC306.5
- net VDD_A: now also C411.2, D321.C; no longer C7.2, D1.C
- net VDD_C: now also D314.K; no longer D413.K
- net VEE_C: now also C396.2, C397.2
- net VREFH0: now also IC400.130; no longer U2.130
- net VREFL0: now also IC400.129; no longer U2.129
- net VSS_USB: now also IC400.37; no longer U2.37
- net V_-5V0_AUX: now also C349.2, C350.2, C368.2, C369.2, C392.2, C408.2, IC307.8, IC311.8
- net V_12V0: now also C204.2, C337.1, C338.2, D201.1; no longer C15.2, R201.2
- net V_12V0_AUX: now also D200.1, R406.1, R418.1; no longer R200.2
- net V_3V3: now also C402.2, C454.1, C456.1, D324.2, IC400.111, IC400.121, IC400.126, IC400.127, IC400.142, IC400.21, IC400.49, IC400.68, IC400.81, IC400.90, IC400.99, R443.2, R444.2, R445.2, R446.2, T307.3, T308.3, T309.3, T310.3, X403.2, X403.4; no longer C401.2, D324.3, Q307.3, Q308.3, Q309.3, Q310.3, R11.2, R12.2, R4.2, R5.2, U2.111, U2.121, U2.126, U2.142, U2.21, U2.49, U2.68, U2.81, U2.90, U2.99, X1.2, X1.4
- net V_5V0: now also IC300.5, R319.2; no longer IC2.5, R3.2
- net V_CS_F: now also D324.3; no longer D324.2
- net V_RECT_F_MINUS: now also C103.2, C104.2, C106.2, C206.1, C207.2, C210.1, C211.1, C335.1, C336.1, C345.1, C349.1, C350.1, C352.1, C365.1, C366.1, C367.1, C368.1, C369.1, C382.1, C387.2, C392.1, C393.2, C394.1, C408.1, C424.1, C426.1, D101.3, D104.A, D317.A, D320.A, IC100.2, IC307.3, IC311.3, R104.1, R110.1, R200.1, R328.1, R330.1, R331.1, R411.2, R423.2, T303.3, X205.5; no longer R328.2
- net WELDER+: now also X2.1, X2.1-1, X2.1-10, X2.1-11, X2.1-12, X2.1-13, X2.1-14, X2.1-15, X2.1-16, X2.1-17, X2.1-18, X2.1-19, X2.1-2, X2.1-20, X2.1-21, X2.1-22, X2.1-23, X2.1-24, X2.1-25, X2.1-26, X2.1-27, X2.1-28, X2.1-29, X2.1-3, X2.1-30, X2.1-31, X2.1-32, X2.1-33, X2.1-34, X2.1-35, X2.1-4, X2.1-5, X2.1-6, X2.1-7, X2.1-8, X2.1-9
- net WELDER-: now also X4.1, X4.1-1, X4.1-10, X4.1-11, X4.1-12, X4.1-13, X4.1-14, X4.1-15, X4.1-16, X4.1-17, X4.1-18, X4.1-19, X4.1-2, X4.1-20, X4.1-21, X4.1-22, X4.1-23, X4.1-24, X4.1-25, X4.1-26, X4.1-27, X4.1-28, X4.1-29, X4.1-3, X4.1-30, X4.1-31, X4.1-32, X4.1-33, X4.1-34, X4.1-35, X4.1-4, X4.1-5, X4.1-6, X4.1-7, X4.1-8, X4.1-9
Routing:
- net GND: track 0.00 -> 1241.9 mm, vias 0 -> 122
- net V_RECT_F_MINUS: track 0.00 -> 978.3 mm, vias 0 -> 33
- net NODE_C: track 0.00 -> 679.6 mm, vias 0 -> 32
- net V_3V3: track 0.00 -> 597.3 mm, vias 0 -> 29
- net N$49: track 0.00 -> 582.9 mm
- net V_12V0_AUX: track 0.00 -> 526.7 mm, vias 0 -> 8
- net DI_G_DRV_RDY: track 0.00 -> 400.5 mm, vias 0 -> 11
- net NDO_G_DRV_RST: track 0.00 -> 364.4 mm, vias 0 -> 5
- net NODE_A: track 0.00 -> 320.3 mm, vias 0 -> 21
- net /G_DRV_FAULTC: track 0.00 -> 261.5 mm, vias 0 -> 3
- net WELDER+: track 0.00 -> 234.9 mm, vias 0 -> 2
- net G_DRV_INC: track 0.00 -> 219.0 mm, vias 0 -> 2
- net WELDER-: track 0.00 -> 209.7 mm
- net /G_DRV_FAULTA: track 0.00 -> 189.0 mm, vias 0 -> 2
- net /G_DRV_FAULTD: track 0.00 -> 188.0 mm, vias 0 -> 3
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- added copper zone on layer 1, net FLOATING
- added copper zone on layer 1, net GND
- added copper zone on layer 16, net GND
- added copper zone on layer 2, net GND
- added copper zone on layer 15, net GND1
- added copper zone on layer 1, net MAINS_L
- added copper zone on layer 16, net MAINS_L
- added copper zone on layer 1, net MAINS_L_FUSED
- added copper zone on layer 16, net MAINS_L_FUSED
- added copper zone on layer 1, net MAINS_N
- added copper zone on layer 16, net MAINS_N
- added copper zone on layer 1, net N$104
- added copper zone on layer 2, net N$104
- added copper zone on layer 16, net N$47
- added copper zone on layer 1, net N$48
- added copper zone on layer 16, net N$48
- added copper zone on layer 2, net N$48
- added copper zone on layer 1, net N$49
- added copper zone on layer 15, net N$49
- added copper zone on layer 16, net N$49
- added copper zone on layer 2, net N$49
- added copper zone on layer 15, net N$50
- added copper zone on layer 15, net N$54
- added copper zone on layer 1, net N$93
- added copper zone on layer 1, net NODE-A
- added copper zone on layer 16, net NODE-A
- added copper zone on layer 1, net NODE_A
- added copper zone on layer 16, net NODE_A
- added copper zone on layer 1, net NODE_C
- added copper zone on layer 16, net NODE_C
- added copper zone on layer 1, net QA_GATE
- added copper zone on layer 16, net QA_GATE
- added copper zone on layer 1, net QC_GATE
- added copper zone on layer 16, net QC_GATE
- added copper zone on layer 1, net QD_GATE
- added copper zone on layer 16, net QD_GATE
- added copper zone on layer 1, net VDD_A
- added copper zone on layer 15, net V_12V0
- added copper zone on layer 1, net V_3V3
- added copper zone on layer 15, net V_3V3
- added copper zone on layer 15, net V_5V0
- added copper zone on layer 1, net V_RECT_F_MINUS
- added copper zone on layer 15, net V_RECT_F_MINUS
- added copper zone on layer 16, net V_RECT_F_MINUS
- added copper zone on layer 1, net V_RECT_F_PLUS
- added copper zone on layer 16, net V_RECT_F_PLUS
- added copper zone on layer 2, net V_RECT_F_PLUS
- added copper zone on layer 1, net WELDER+
- added copper zone on layer 16, net WELDER+
- added copper zone on layer 2, net WELDER+
- added copper zone on layer 15, net WELDER+1
- added copper zone on layer 1, net WELDER-
- added copper zone on layer 16, net WELDER-
- added copper zone on layer 2, net WELDER-
- added copper zone on layer 15, net WELDER-1
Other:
- board size 160 x 100 mm -> 395 x 232 mm
- board text added: "High Voltage"
- board text added: "Welder PSU HW05.xx"

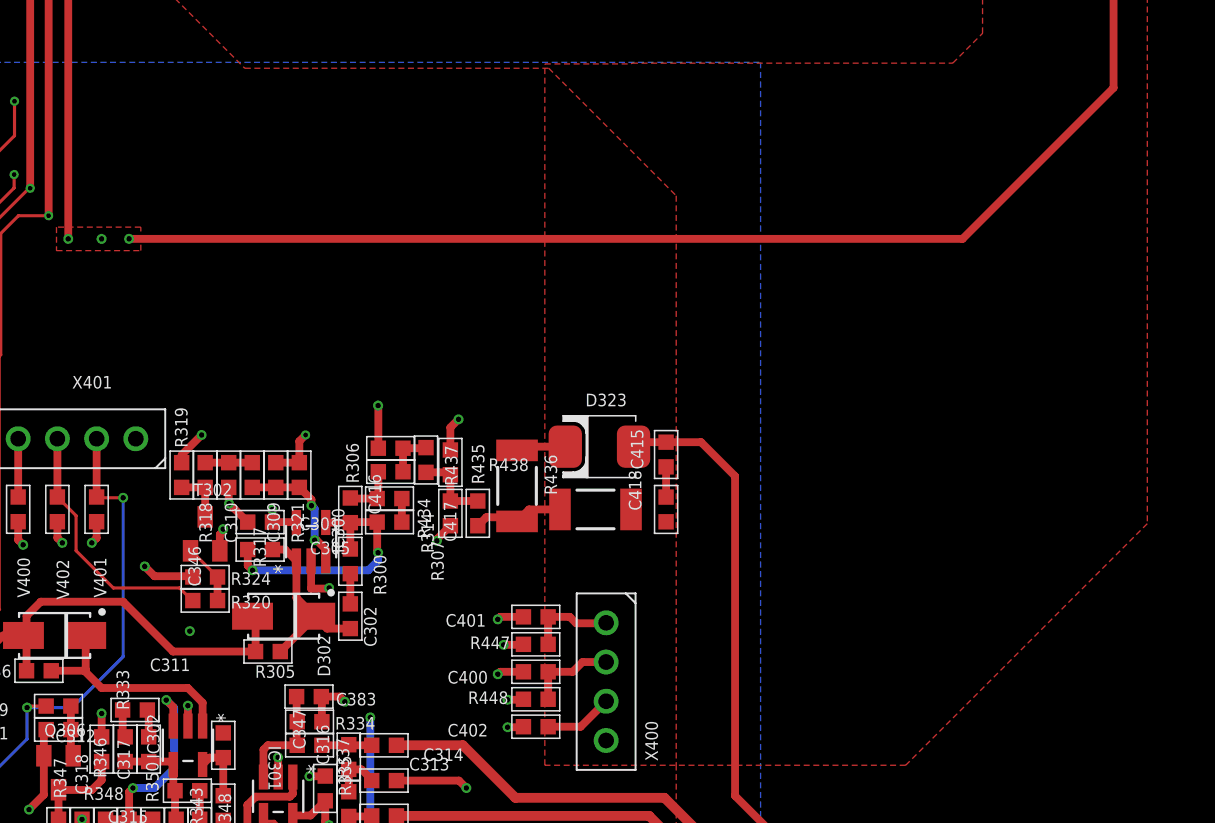
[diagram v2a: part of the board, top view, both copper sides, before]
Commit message: Welder PSU HW05.05
Transferring into Eagle Done.
Via Stitching, DRC still open
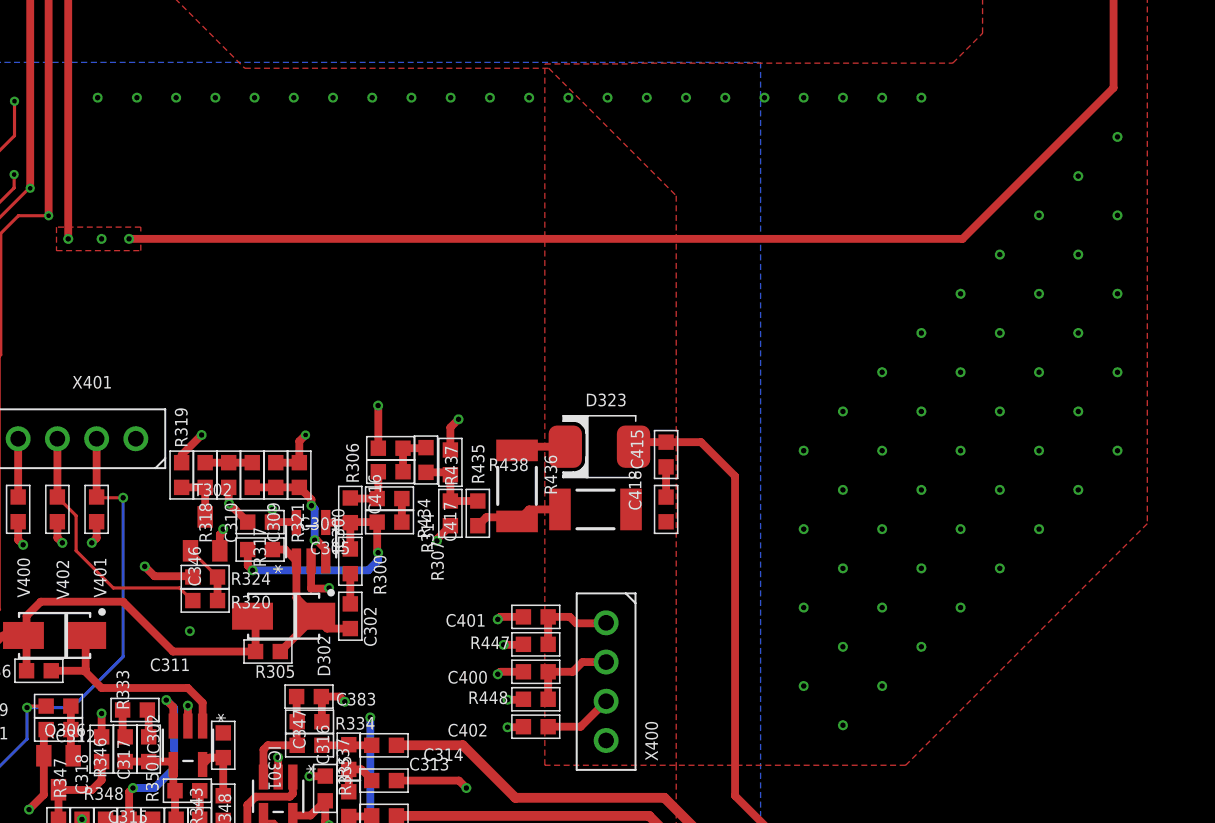
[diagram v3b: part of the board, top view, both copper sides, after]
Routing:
- net GND: vias 122 -> 188
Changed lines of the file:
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@@
 <drawing>
 <settings>
-<setting alwaysvectorfont="yes"/>
+<setting alwaysvectorfont="no"/>
 <setting verticaltext="up"/>
 </settings>
-<grid distance="5" unitdist="mil" unit="mil" style="lines" multiple="1" display="yes" altdistance="2" altunitdist="mil" altunit="mil"/>
+<grid distance="100" unitdist="mil" unit="mil" style="lines" multiple="1" display="yes" altdistance="2" altunitdist="mil" altunit="mil"/>
 <layers>
 <layer number="1" name="Top" color="4" fill="1" visible="yes" active="yes"/>
@@
 </polygon>
 <via x="173.609" y="46.736" extent="1-16" drill="0.35"/>
+<via x="215.9" y="81.28" extent="1-16" drill="0.35"/>
+<via x="213.36" y="81.28" extent="1-16" drill="0.35"/>
+<via x="210.82" y="81.28" extent="1-16" drill="0.35"/>
+<via x="208.28" y="81.28" extent="1-16" drill="0.35"/>
+<via x="205.74" y="81.28" extent="1-16" drill="0.35"/>
+<via x="203.2" y="81.28" extent="1-16" drill="0.35"/>
+<via x="200.66" y="81.28" extent="1-16" drill="0.35"/>
+<via x="198.12" y="81.28" extent="1-16" drill="0.35"/>
+<via x="195.58" y="81.28" extent="1-16" drill="0.35"/>
+<via x="190.5" y="81.28" extent="1-16" drill="0.35"/>
+<via x="193.04" y="81.28" extent="1-16" drill="0.35"/>
+<via x="187.96" y="81.28" extent="1-16" drill="0.35"/>
+<via x="185.42" y="81.28" extent="1-16" drill="0.35"/>
+<via x="182.88" y="81.28" extent="1-16" drill="0.35"/>
+<via x="180.34" y="81.28" extent="1-16" drill="0.35"/>
+<via x="177.8" y="81.28" extent="1-16" drill="0.35"/>
+<via x="175.26" y="81.28" extent="1-16" drill="0.35"/>
+<via x="172.72" y="81.28" extent="1-16" drill="0.35"/>
+<via x="170.18" y="81.28" extent="1-16" drill="0.35"/>
+<via x="167.64" y="81.28" extent="1-16" drill="0.35"/>
+<via x="218.44" y="81.28" extent="1-16" drill="0.35"/>
+<via x="220.98" y="81.28" extent="1-16" drill="0.35"/>
+<via x="220.98" y="60.96" extent="1-16" drill="0.35"/>
+<via x="226.06" y="71.12" extent="1-16" drill="0.35"/>
+<via x="228.6" y="73.66" extent="1-16" drill="0.35"/>
+<via x="231.14" y="76.2" extent="1-16" drill="0.35"/>
+<via x="233.68" y="78.74" extent="1-16" drill="0.35"/>
+<via x="233.68" y="73.66" extent="1-16" drill="0.35"/>
+<via x="233.68" y="68.58" extent="1-16" drill="0.35"/>
+<via x="231.14" y="71.12" extent="1-16" drill="0.35"/>
+<via x="231.14" y="66.04" extent="1-16" drill="0.35"/>
+<via x="233.68" y="63.5" extent="1-16" drill="0.35"/>
+<via x="228.6" y="68.58" extent="1-16" drill="0.35"/>
+<via x="228.6" y="63.5" extent="1-16" drill="0.35"/>
+<via x="226.06" y="66.04" extent="1-16" drill="0.35"/>
+<via x="226.06" y="60.96" extent="1-16" drill="0.35"/>
+<via x="231.14" y="60.96" extent="1-16" drill="0.35"/>
+<via x="223.52" y="68.58" extent="1-16" drill="0.35"/>
+<via x="223.52" y="63.5" extent="1-16" drill="0.35"/>
+<via x="223.52" y="58.42" extent="1-16" drill="0.35"/>
+<via x="226.06" y="55.88" extent="1-16" drill="0.35"/>
+<via x="231.14" y="55.88" extent="1-16" drill="0.35"/>
+<via x="233.68" y="58.42" extent="1-16" drill="0.35"/>
+<via x="228.6" y="58.42" extent="1-16" drill="0.35"/>
+<via x="228.6" y="53.34" extent="1-16" drill="0.35"/>
+<via x="226.06" y="50.8" extent="1-16" drill="0.35"/>
+<via x="223.52" y="53.34" extent="1-16" drill="0.35"/>
+<via x="223.52" y="48.26" extent="1-16" drill="0.35"/>
+<via x="220.98" y="66.04" extent="1-16" drill="0.35"/>
+<via x="218.44" y="63.5" extent="1-16" drill="0.35"/>
+<via x="220.98" y="55.88" extent="1-16" drill="0.35"/>
+<via x="220.98" y="50.8" extent="1-16" drill="0.35"/>
+<via x="220.98" y="45.72" extent="1-16" drill="0.35"/>
+<via x="215.9" y="60.96" extent="1-16" drill="0.35"/>
+<via x="213.36" y="58.42" extent="1-16" drill="0.35"/>
+<via x="218.44" y="58.42" extent="1-16" drill="0.35"/>
+<via x="215.9" y="55.88" extent="1-16" drill="0.35"/>
+<via x="213.36" y="53.34" extent="1-16" drill="0.35"/>
+<via x="218.44" y="53.34" extent="1-16" drill="0.35"/>
+<via x="215.9" y="50.8" extent="1-16" drill="0.35"/>
+<via x="218.44" y="48.26" extent="1-16" drill="0.35"/>
+<via x="215.9" y="45.72" extent="1-16" drill="0.35"/>
+<via x="218.44" y="43.18" extent="1-16" drill="0.35"/>
+<via x="215.9" y="40.64" extent="1-16" drill="0.35"/>
+<via x="213.36" y="43.18" extent="1-16" drill="0.35"/>
+<via x="213.36" y="48.26" extent="1-16" drill="0.35"/>
 <wire x1="161.533790625" y1="15.14599375" x2="157.607" y2="16.637" width="0" layer="19" extent="1-1"/>
 <wire x1="159.676590625" y1="121.74481875" x2="159.676590625" y2="132.7428125" width="0" layer="19" extent="1-1"/>
